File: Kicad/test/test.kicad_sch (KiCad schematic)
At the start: 67 parts, among them J1 SPKOUT, J2 PrgmUART, J3 USB_C_Receptacle_PowerOnly_6P, SW1 SW_Push, SW2 SW_Push, SW3 SW_Push, SW4 SW_Push, SW5 SW_Push, U1 MAX98357A, U2 ESP32-S3-WROOM-1

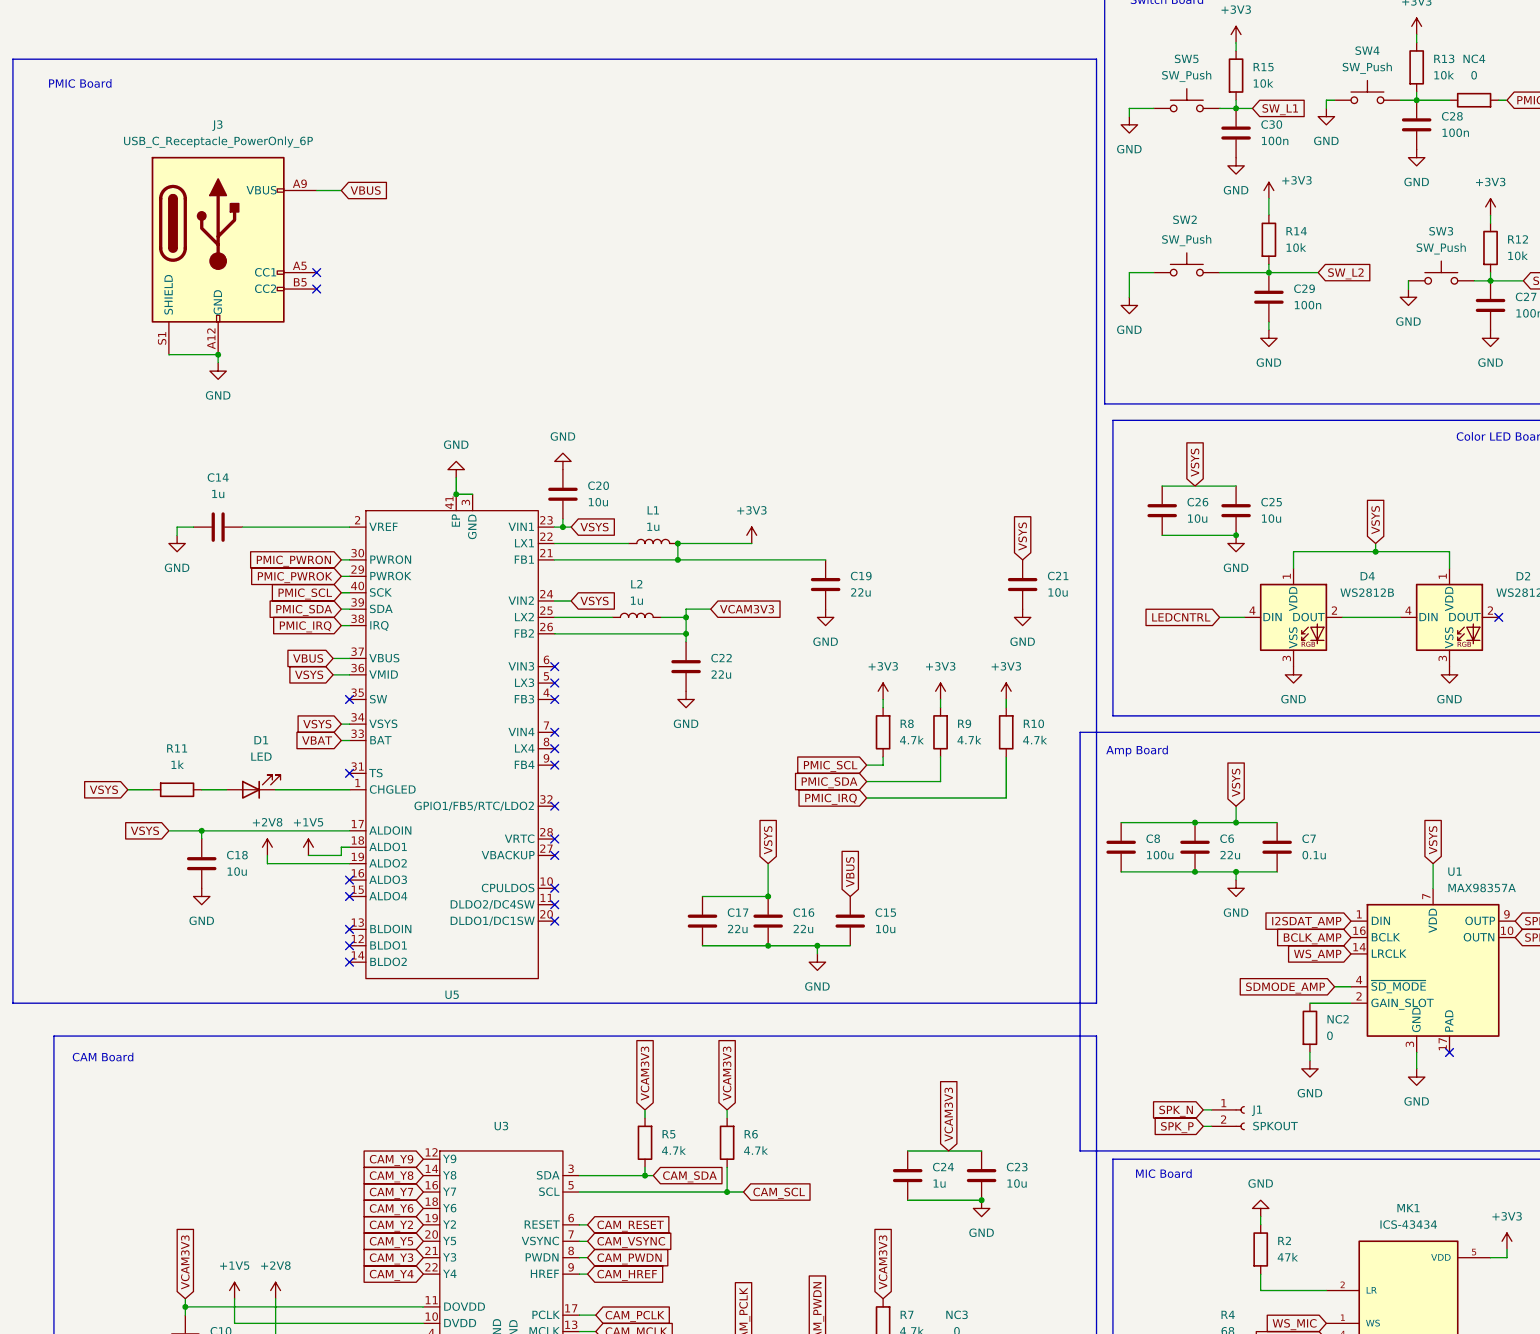
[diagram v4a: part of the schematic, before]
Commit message: Added Battery plugin in schematic
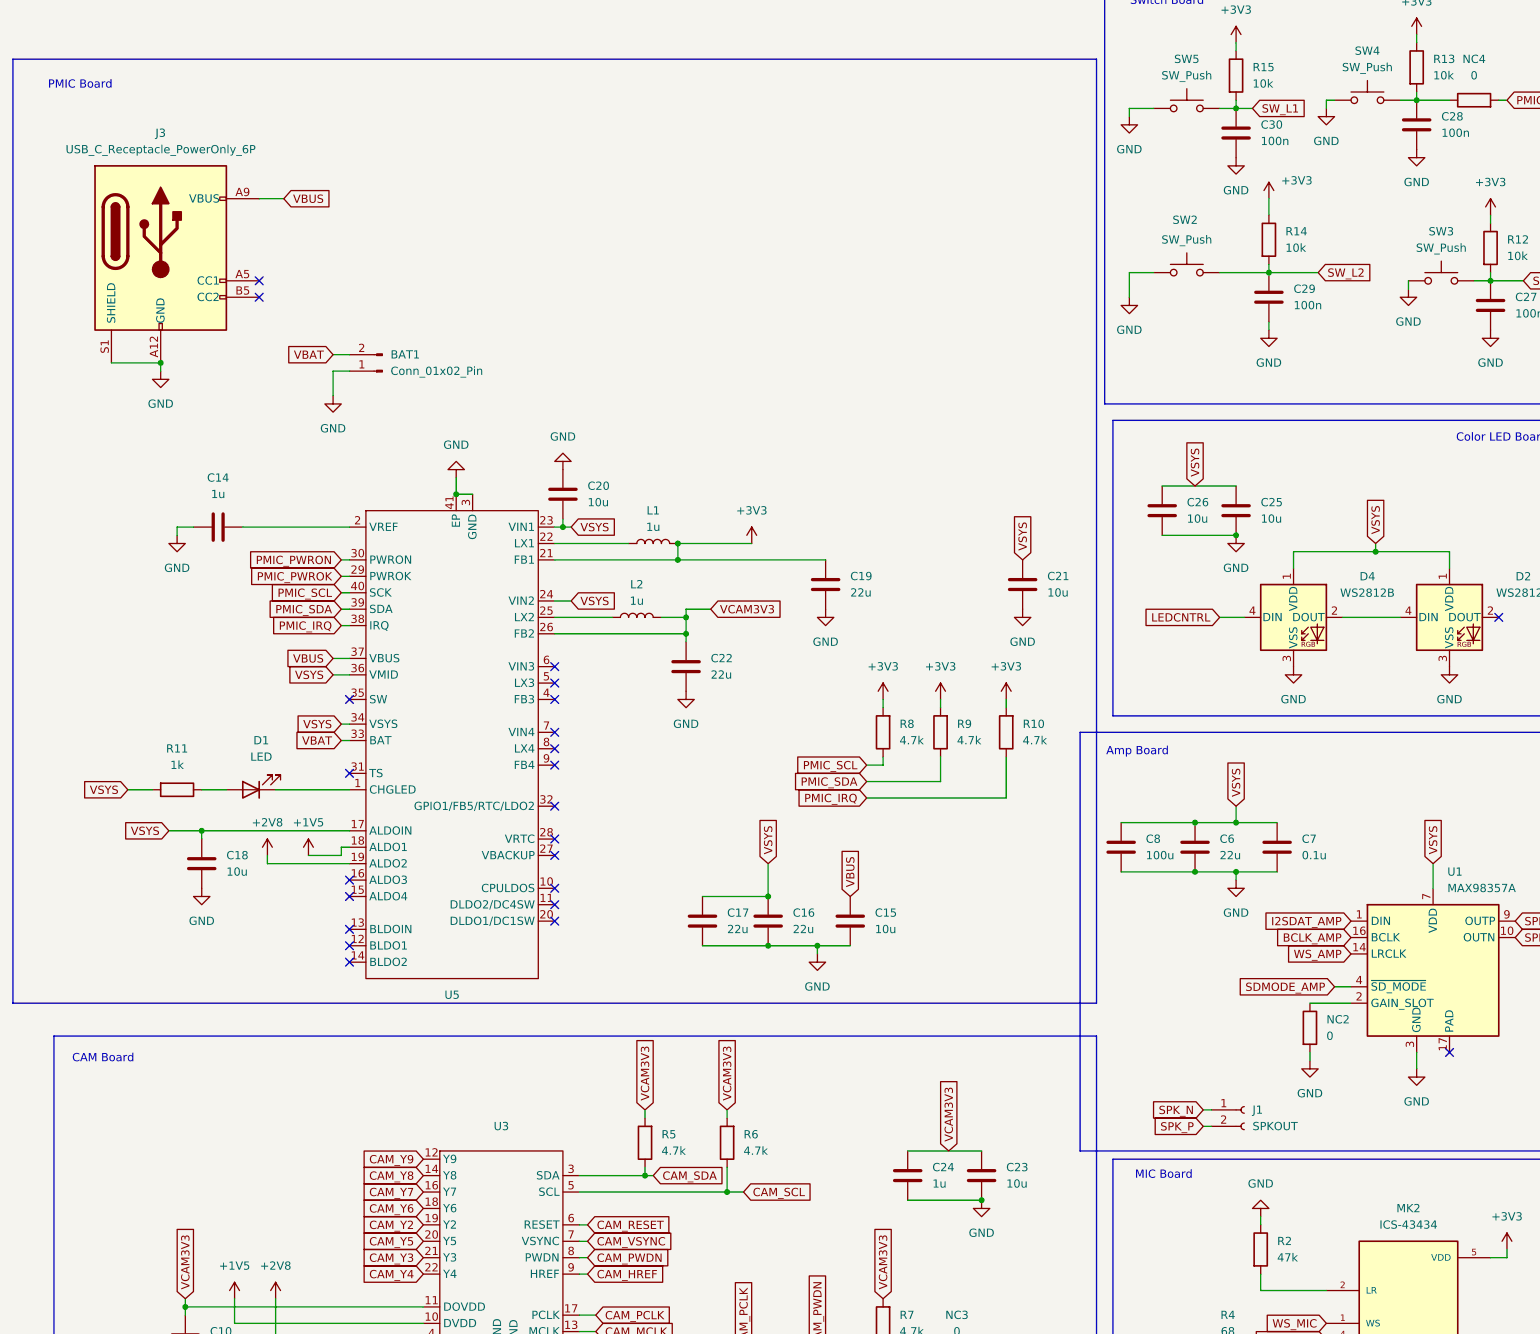
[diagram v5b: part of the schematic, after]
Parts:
- removed MK1: ICS-43434, ICS-43434:MIC_ICS-43434, symbol Components_Wareit_Mic:ICS-43434
- added BAT1: Conn_01x02_Pin, symbol Connector:Conn_01x02_Pin
- added MK2: ICS-43434, ICS-43434:MIC_ICS-43434, symbol Components_Wareit_Mic:ICS-43434
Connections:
- net +3V3: now also MK2.5 (VDD)
- net BCLK_MIC: now also MK2.4 (SCK)
- net GND: now also BAT1.1 (Pin_1), MK2.3 (GND)
- net VBAT: now also BAT1.2 (Pin_2)
- net WS_MIC: now also MK2.1 (WS)
- net at R2.2: now also MK2.2 (LR)
- net at R3.1, R4.2: now also MK2.6 (SD)
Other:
- moved on the sheet: J3

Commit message: Started PCB Layout designs
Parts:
- removed J3: USB_C_Receptacle_PowerOnly_6P, symbol Connector:USB_C_Receptacle_PowerOnly_6P
- added P1: USB_C_Plug_USB2.0, Connector_USB:USB_C_Receptacle_HRO_TYPE-C-31-M-12, symbol Connector:USB_C_Plug_USB2.0
- added R16: 1M, Resistor_SMD:R_0805_2012Metric_Pad1.20x1.40mm_HandSolder, symbol Device:R
- BAT1, J1: footprint (none) -> Connector_PinHeader_2.54mm:PinHeader_1x02_P2.54mm_Vertical
- C1, C10, C11, C12, C13, C14, C15, C16, C17, C18, C19, C2, C20, C21, C22, C23, C24, C25, C26, C27, C28, C29, C3, C30, C4, C5, C6, C7, C8, C9, L1, L2: footprint (none) -> Capacitor_SMD:C_0805_2012Metric_Pad1.18x1.45mm_HandSolder
- D1: footprint (none) -> LED_SMD:LED_0201_0603Metric
- J2: footprint (none) -> Connector_PinHeader_2.54mm:PinHeader_1x06_P2.54mm_Vertical
- MK2: footprint ICS-43434:MIC_ICS-43434 -> Sensor_Audio:InvenSense_ICS-43434-6_3.5x2.65mm
- NC1, NC2, NC3, NC4: footprint (none) -> Resistor_SMD:R_1206_3216Metric; now not fitted
- R1, R10, R11, R12, R13, R14, R15, R2, R3, R4, R5, R6, R7, R8, R9: footprint (none) -> Resistor_SMD:R_0805_2012Metric_Pad1.20x1.40mm_HandSolder
- SW1, SW5: footprint (none) -> Button_Switch_SMD:SW_SPST_B3S-1000
- SW2, SW3, SW4: footprint (none) -> switchLibrary:K2-1114SA-A4SW-06
- U3: footprint (none) -> Connector_FFC-FPC:TE_2-1734839-4_1x24-1MP_P0.5mm_Horizontal
- U5: footprint (none) -> Package_DFN_QFN:QFN-40-1EP_5x5mm_P0.4mm_EP3.6x3.6mm
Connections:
- net GND: now also P1.A1 (GND), P1.A12 (GND), P1.B1 (GND), P1.B12 (GND), R16.2
- net VBUS: now also P1.A4 (VBUS), P1.A9 (VBUS), P1.B4 (VBUS), P1.B9 (VBUS)
- new net: P1.S1 (SHIELD), R16.1
- no-connect marks 24 -> 26

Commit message: Placed components on PCB
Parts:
- C1, C10, C11, C12, C13, C14, C15, C16, C17, C18, C19, C2, C20, C21, C22, C23, C24, C25, C26, C27, C28, C29, C3, C30, C4, C5, C6, C7, C8, C9, L1, L2: footprint Capacitor_SMD:C_0805_2012Metric_Pad1.18x1.45mm_HandSolder -> Capacitor_SMD:C_0603_1608Metric_Pad1.08x0.95mm_HandSolder
- R1, R10, R11, R12, R13, R14, R15, R16, R2, R3, R4, R5, R6, R7, R8, R9: footprint Resistor_SMD:R_0805_2012Metric_Pad1.20x1.40mm_HandSolder -> Resistor_SMD:R_0603_1608Metric_Pad0.98x0.95mm_HandSolder
